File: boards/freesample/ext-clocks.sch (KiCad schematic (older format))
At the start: 43 parts

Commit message: Continued work on schematic capture
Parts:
- J3, J4, J5: renamed from J?; symbol conn:CONN_COAXIAL -> freesample-rescue:CONN_COAXIAL-conn
- gave numbers to parts that had none: 40

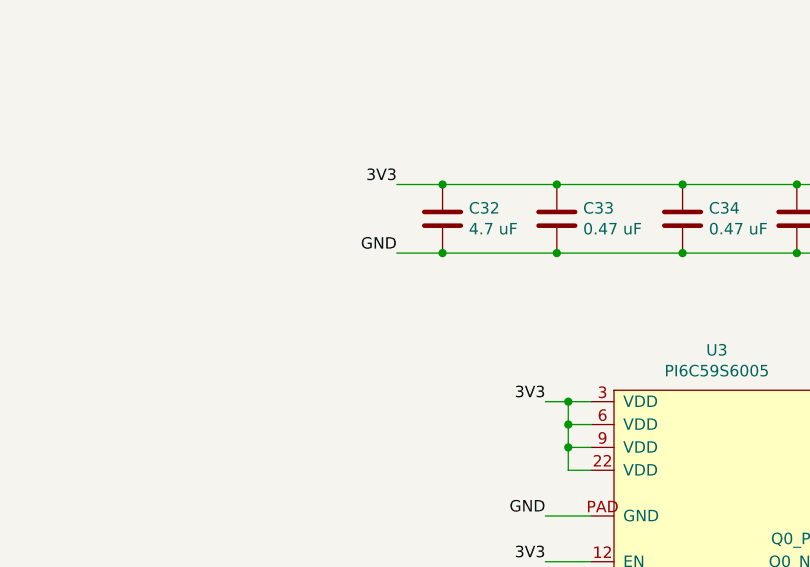
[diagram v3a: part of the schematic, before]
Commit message: Hooked up new power rails
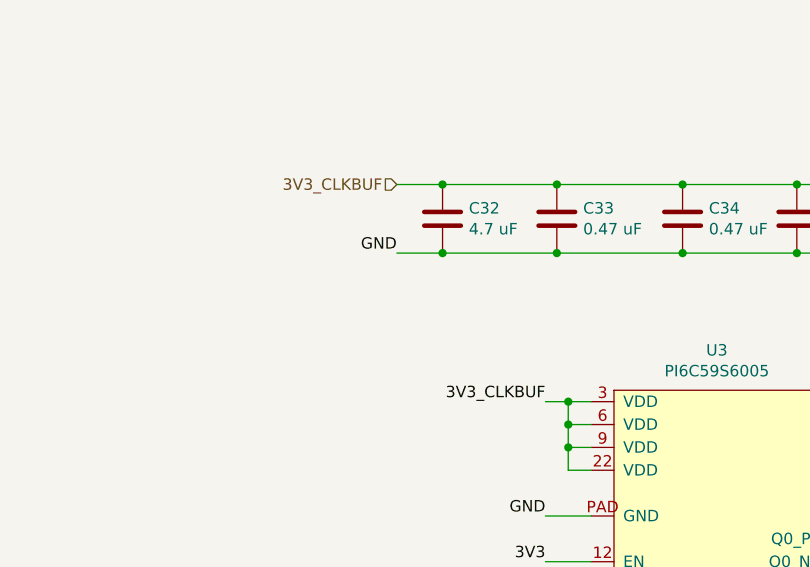
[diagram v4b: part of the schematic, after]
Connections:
- net 3V3: no longer C32.1, C33.1, C34.1, C35.1, C36.1, U3.22 (VDD), U3.3 (VDD), U3.6 (VDD), U3.9 (VDD)
- new net 3V3_CLKBUF: C32.1, C33.1, C34.1, C35.1, C36.1, U3.22 (VDD), U3.3 (VDD), U3.6 (VDD), U3.9 (VDD)
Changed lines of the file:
@@
 Sheet 2 12
 Title "FREESAMPLE Oscilloscope"
-Date "2019-02-23"
+Date "2019-02-26"
 Rev "0.1"
 Comp "Andrew D. Zonenberg / Antikernel Labs"
@@
 Wire Wire Line
 	6650 3050 6150 3050
-Text Label 5950 2750 2    50   ~ 0
-3V3
 Wire Wire Line
 	5950 2750 6150 2750
@@
 Text Label 6300 5800 0    50   ~ 0
 REFCLK1_AC_N
-Text Label 6600 3700 2    50   ~ 0
-3V3
 Wire Wire Line
 	6600 3700 6700 3700
@@
 Text HLabel 7900 5000 2    50   Output ~ 0
 CDR_EXTCLK_N
+Text HLabel 5950 2750 0    50   Input ~ 0
+3V3_CLKBUF
+Text Label 6600 3700 2    50   ~ 0
+3V3_CLKBUF
 $EndSCHEMATC

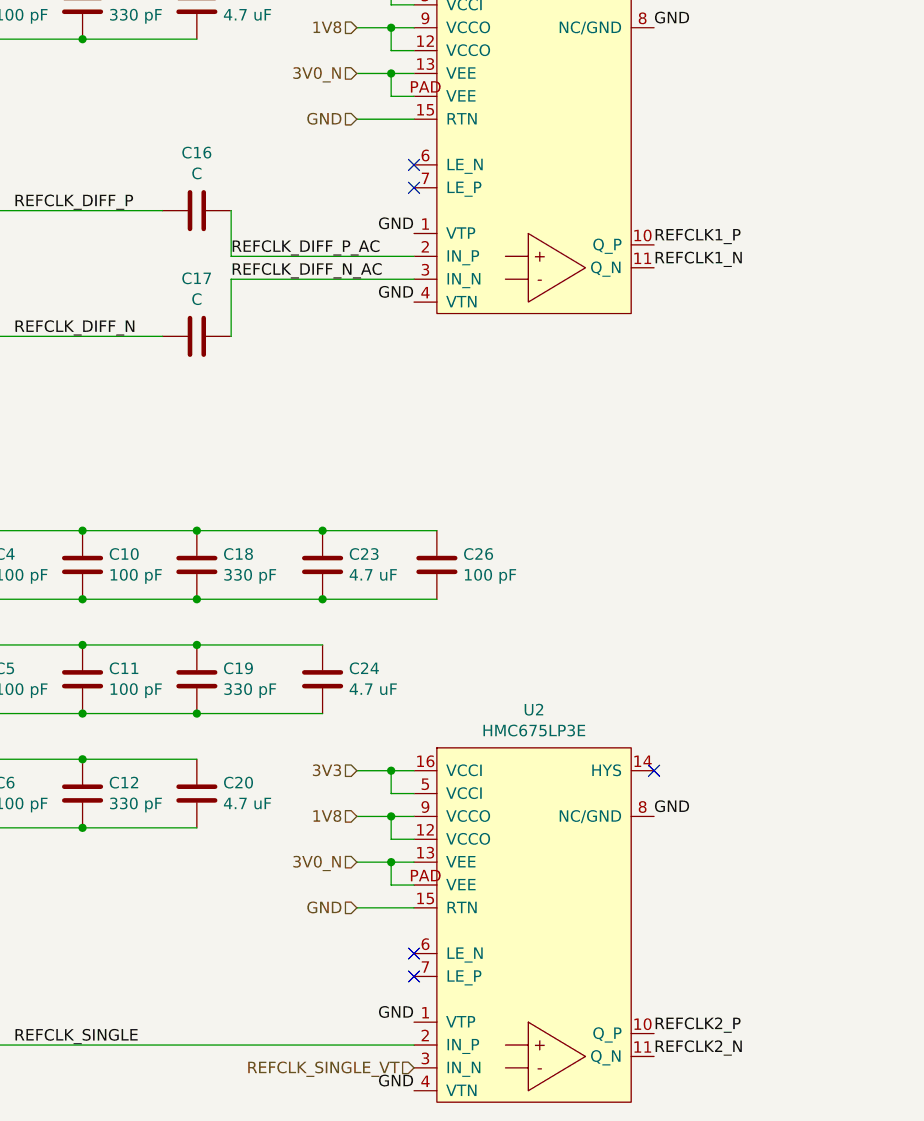
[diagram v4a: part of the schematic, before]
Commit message: Continued schematic capture work. Hooked up most SoM connectors.
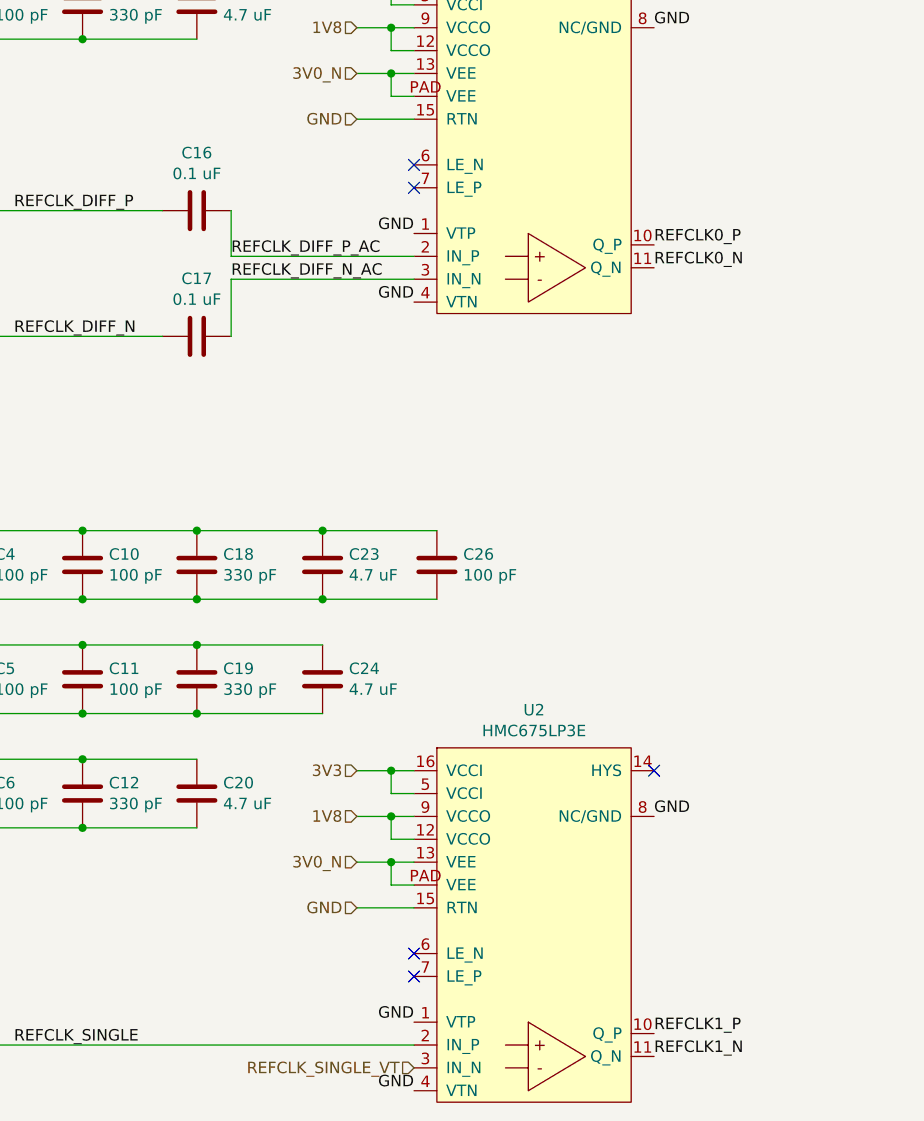
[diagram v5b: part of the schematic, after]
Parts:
- C16, C17: value C -> 0.1 uF
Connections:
- net REFCLK2_N is gone; now on net REFCLK1_N: U2.11 (Q_N)
- net REFCLK2_P is gone; now on net REFCLK1_P: U2.10 (Q_P)
- net REFCLK0_N: now also U1.11 (Q_N)
- net REFCLK0_P: now also U1.10 (Q_P)
- net REFCLK1_N: no longer U1.11 (Q_N)
- net REFCLK1_P: no longer U1.10 (Q_P)
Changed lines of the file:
@@
 Sheet 2 12
 Title "FREESAMPLE Oscilloscope"
-Date "2019-02-26"
+Date "2019-03-10"
 Rev "0.1"
 Comp "Andrew D. Zonenberg / Antikernel Labs"
 Comment1 "External reference clocks"
-Comment2 ""
+Comment2 "Ready for review"
 Comment3 ""
 Comment4 ""
@@
 P 1750 2700
 F 0 "C16" V 1498 2700 50  0000 C CNN
-F 1 "C" V 1589 2700 50  0000 C CNN
+F 1 "0.1 uF" V 1589 2700 50  0000 C CNN
 F 2 "" H 1788 2550 50  0001 C CNN
 F 3 "" H 1750 2700 50  0001 C CNN
@@
 P 1750 3250
 F 0 "C17" V 1498 3250 50  0000 C CNN
-F 1 "C" V 1589 3250 50  0000 C CNN
+F 1 "0.1 uF" V 1589 3250 50  0000 C CNN
 F 2 "" H 1788 3100 50  0001 C CNN
 F 3 "" H 1750 3250 50  0001 C CNN
@@
 REFCLK_DIFF_N_AC
 Text Label 3750 2850 0    50   ~ 0
-REFCLK1_P
+REFCLK0_P
 Text Label 3750 2950 0    50   ~ 0
-REFCLK1_N
+REFCLK0_N
 Text HLabel 2450 1700 0    50   Input ~ 0
 3V3
@@
 $EndComp
 Text Label 3750 6300 0    50   ~ 0
-REFCLK2_P
+REFCLK1_P
 Text Label 3750 6400 0    50   ~ 0
-REFCLK2_N
+REFCLK1_N
 Text HLabel 2450 5150 0    50   Input ~ 0
 3V3

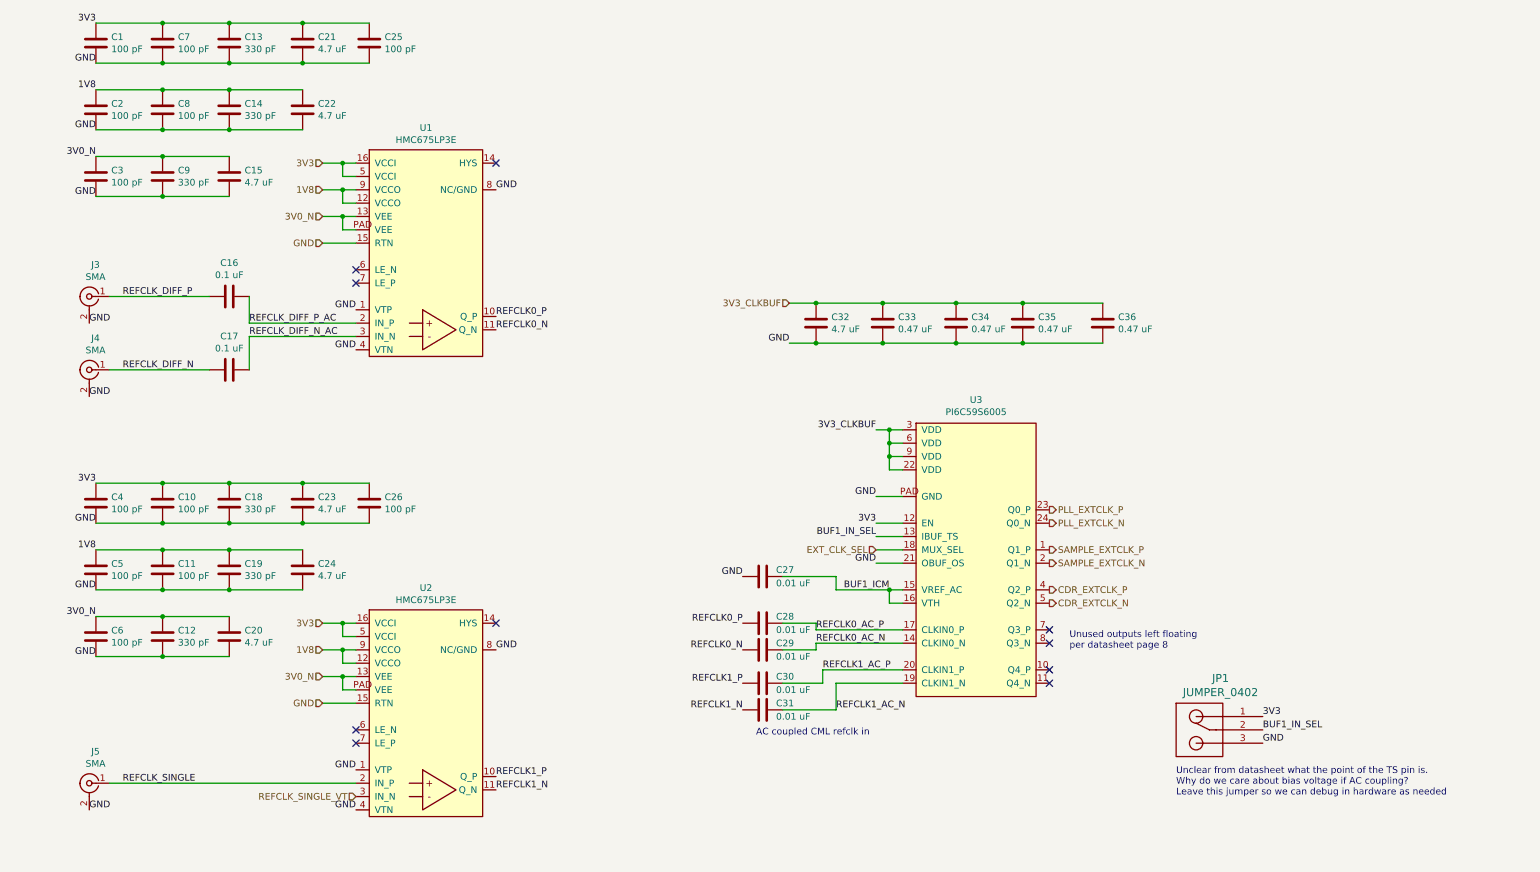
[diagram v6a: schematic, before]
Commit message: Specified part number for AC coupling caps
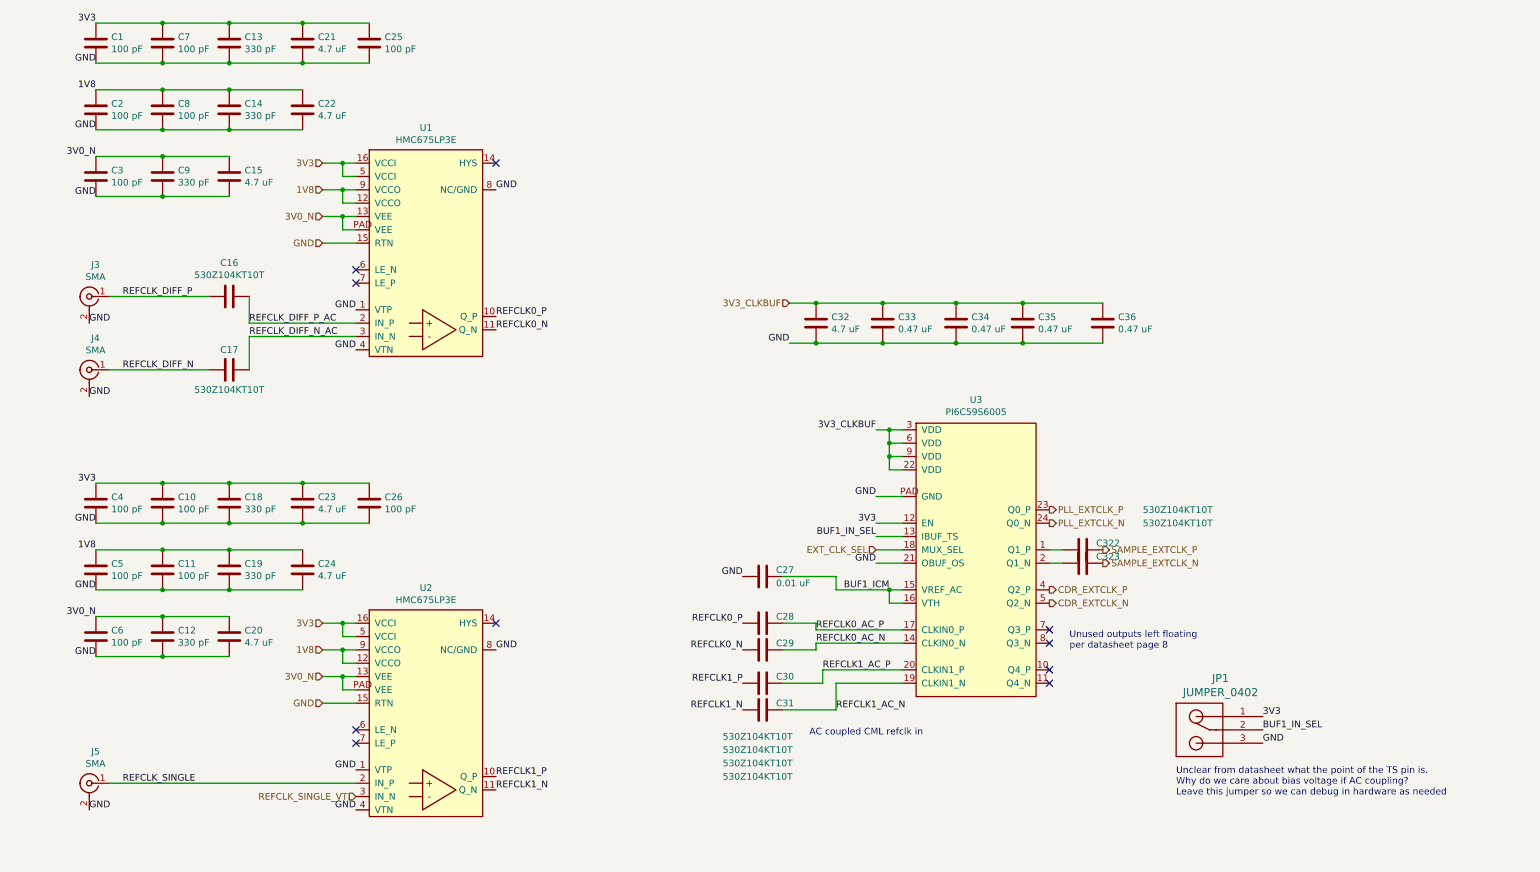
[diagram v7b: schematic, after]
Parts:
- added C322, C323: 530Z104KT10T, symbol device:C
- C16, C17: value 0.1 uF -> 530Z104KT10T
- C28, C29, C30, C31: value 0.01 uF -> 530Z104KT10T
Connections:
- net SAMPLE_EXTCLK_N: now also C323.1; no longer U3.2 (Q1_N)
- net SAMPLE_EXTCLK_P: now also C322.1; no longer U3.1 (Q1_P)
- new net: C322.2, U3.1 (Q1_P)
- new net: C323.2, U3.2 (Q1_N)
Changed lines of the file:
@@
 Sheet 2 12
 Title "FREESAMPLE Oscilloscope"
-Date "2019-03-11"
+Date "2019-03-13"
 Rev "0.1"
 Comp "Andrew D. Zonenberg / Antikernel Labs"
@@
 P 1750 2700
 F 0 "C16" V 1498 2700 50  0000 C CNN
-F 1 "0.1 uF" V 1589 2700 50  0000 C CNN
+F 1 "530Z104KT10T" V 1589 2700 50  0000 C CNN
 F 2 "" H 1788 2550 50  0001 C CNN
 F 3 "" H 1750 2700 50  0001 C CNN
@@
 U 1 1 5C0ED600
 P 1750 3250
-F 0 "C17" V 1498 3250 50  0000 C CNN
-F 1 "0.1 uF" V 1589 3250 50  0000 C CNN
+F 0 "C17" V 1600 3250 50  0000 C CNN
+F 1 "530Z104KT10T" V 1900 3250 50  0000 C CNN
 F 2 "" H 1788 3100 50  0001 C CNN
 F 3 "" H 1750 3250 50  0001 C CNN
@@
 P 5750 5150
 F 0 "C28" V 5700 5250 50  0000 L CNN
-F 1 "0.01 uF" V 5800 5250 50  0000 L CNN
+F 1 "530Z104KT10T" V 6600 4850 50  0000 L CNN
 F 2 "" H 5788 5000 50  0001 C CNN
 F 3 "" H 5750 5150 50  0001 C CNN
@@
 P 5750 5350
 F 0 "C29" V 5700 5450 50  0000 L CNN
-F 1 "0.01 uF" V 5800 5450 50  0000 L CNN
+F 1 "530Z104KT10T" V 6500 5050 50  0000 L CNN
 F 2 "" H 5788 5200 50  0001 C CNN
 F 3 "" H 5750 5350 50  0001 C CNN
@@
 P 5750 5600
 F 0 "C30" V 5700 5700 50  0000 L CNN
-F 1 "0.01 uF" V 5800 5700 50  0000 L CNN
+F 1 "530Z104KT10T" V 6350 5300 50  0000 L CNN
 F 2 "" H 5788 5450 50  0001 C CNN
 F 3 "" H 5750 5600 50  0001 C CNN
@@
 P 5750 5800
 F 0 "C31" V 5700 5900 50  0000 L CNN
-F 1 "0.01 uF" V 5800 5900 50  0000 L CNN
+F 1 "530Z104KT10T" V 6250 5500 50  0000 L CNN
 F 2 "" H 5788 5650 50  0001 C CNN
 F 3 "" H 5750 5800 50  0001 C CNN
@@
 Wire Wire Line
 	6600 4700 6800 4700
-Text Notes 5700 6000 0    50   ~ 0
+Text Notes 6100 6000 0    50   ~ 0
 AC coupled CML refclk in
 Wire Wire Line
@@
 Wire Wire Line
 	6600 4600 6800 4600
-Text HLabel 7900 4600 2    50   Output ~ 0
+Text HLabel 8300 4600 2    50   Output ~ 0
 SAMPLE_EXTCLK_P
-Text HLabel 7900 4700 2    50   Output ~ 0
+Text HLabel 8300 4700 2    50   Output ~ 0
 SAMPLE_EXTCLK_N
 NoConn ~ 7900 5200
@@
 Text Label 6600 3700 2    50   ~ 0
 3V3_CLKBUF
+$Comp
+L device:C C322
+U 1 1 5D42D3BC
+P 8150 4600
+F 0 "C322" V 8100 4700 50  0000 L CNN
+F 1 "530Z104KT10T" V 7850 5050 50  0000 L CNN
+F 2 "" H 8188 4450 50  0001 C CNN
+F 3 "" H 8150 4600 50  0001 C CNN
+	1    8150 4600
+	0    1    1    0
+$EndComp
+$Comp
+L device:C C323
+U 1 1 5D42E37F
+P 8150 4700
+F 0 "C323" V 8100 4800 50  0000 L CNN
+F 1 "530Z104KT10T" V 7850 5150 50  0000 L CNN
+F 2 "" H 8188 4550 50  0001 C CNN
+F 3 "" H 8150 4700 50  0001 C CNN
+	1    8150 4700
+	0    1    1    0
+$EndComp
+Wire Wire Line
+	8000 4600 7900 4600
+Wire Wire Line
+	7900 4700 8000 4700
 $EndSCHEMATC
